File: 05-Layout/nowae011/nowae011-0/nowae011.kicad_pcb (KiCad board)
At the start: 2 copper layers, 25.4 x 18.4 mm, 15 parts, among them P1 VIN, P2 VOUT, U1 ST1S14PHR

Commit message: Updated pcb (nowae011-0)
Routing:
- net Net-(P2-Pad2): track 0.00 -> 1.76 mm
- net +5V: track 14.0 -> 15.8 mm
- net GND: track 17.8 -> 19.2 mm
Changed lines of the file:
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@@
     (thickness 1.6)
     (drawings 30)
-    (tracks 52)
+    (tracks 55)
     (zones 0)
     (modules 15)
@@
     (0 F.Cu signal)
     (31 B.Cu signal)
-    (32 B.Adhes user hide)
-    (33 F.Adhes user hide)
-    (34 B.Paste user hide)
-    (35 F.Paste user hide)
+    (32 B.Adhes user)
+    (33 F.Adhes user)
+    (34 B.Paste user)
+    (35 F.Paste user)
     (36 B.SilkS user)
     (37 F.SilkS user)
-    (38 B.Mask user hide)
-    (39 F.Mask user hide)
+    (38 B.Mask user)
+    (39 F.Mask user)
     (40 Dwgs.User user)
-    (41 Cmts.User user hide)
-    (42 Eco1.User user hide)
-    (43 Eco2.User user hide)
+    (41 Cmts.User user)
+    (42 Eco1.User user)
+    (43 Eco2.User user)
     (44 Edge.Cuts user)
-    (45 Margin user hide)
-    (46 B.CrtYd user hide)
-    (47 F.CrtYd user hide)
-    (48 B.Fab user hide)
+    (45 Margin user)
+    (46 B.CrtYd user)
+    (47 F.CrtYd user)
+    (48 B.Fab user)
     (49 F.Fab user)
   )
   (setup
-    (last_trace_width 0.25)
+    (last_trace_width 1)
     (user_trace_width 0.25)
     (user_trace_width 0.5)
@@
   (gr_line (start 25.4 -13.335) (end 25.4 -5.715) (layer Edge.Cuts) (width 0.15))
   (gr_line (start 0 -5.715) (end 0 -13.335) (layer Edge.Cuts) (width 0.15))
-  (segment (start 2.54 -12.085) (end 0.40001 -12.085) (width 0.25) (layer F.Cu) (net 1))
+  (segment (start 2.54 -12.085) (end 0.77501 -12.085) (width 1) (layer F.Cu) (net 1))
   (via (at 8.255 -6.985) (size 0.6) (drill 0.3) (layers F.Cu B.Cu) (net 2) (status 40000))
   (via (at 10.287 -6.985) (size 0.6) (drill 0.3) (layers F.Cu B.Cu) (net 2) (status 40000))
@@
   (segment (start 2.74 -6.805) (end 2.54 -7.005) (width 1) (layer F.Cu) (net 2))
   (segment (start 4.953 -6.805) (end 2.74 -6.805) (width 1) (layer F.Cu) (net 2))
-  (segment (start 2.54 -7.005) (end 0.40001 -7.005) (width 0.25) (layer F.Cu) (net 2))
   (segment (start 19.217 -16.343) (end 20.32 -15.24) (width 1) (layer F.Cu) (net 2))
   (via (at 20.32 -15.24) (size 1.2) (drill 0.6) (layers F.Cu B.Cu) (net 2))
@@
   (segment (start 6.571 -9.525) (end 8.255 -9.525) (width 0.5) (layer F.Cu) (net 2))
   (segment (start 11.971 -9.525) (end 10.287 -9.525) (width 0.5) (layer F.Cu) (net 2))
+  (segment (start 22.86 -6.965) (end 24.62499 -6.965) (width 1) (layer F.Cu) (net 2))
+  (segment (start 2.54 -7.005) (end 0.77501 -7.005) (width 1) (layer F.Cu) (net 2))
   (segment (start 11.971 -6.985) (end 11.971 -6.185) (width 0.5) (layer F.Cu) (net 3))
   (segment (start 11.971 -6.153) (end 11.971 -6.185) (width 0.5) (layer F.Cu) (net 3))
@@
   (segment (start 15.327 -11.343) (end 14.605 -12.065) (width 0.25) (layer F.Cu) (net 5))
   (segment (start 14.605 -13.6875) (end 13.6255 -14.667) (width 0.25) (layer F.Cu) (net 5))
+  (segment (start 22.86 -12.045) (end 24.62499 -12.045) (width 1) (layer F.Cu) (net 5))
   (segment (start 13.5255 -16.067) (end 12.319 -16.067) (width 0.25) (layer F.Cu) (net 6))
-  (segment (start 2.54 -9.545) (end 0.40001 -9.545) (width 0.25) (layer F.Cu) (net 7))
+  (segment (start 2.54 -9.545) (end 0.77501 -9.545) (width 1) (layer F.Cu) (net 7))
+  (segment (start 22.86 -9.505) (end 24.62499 -9.505) (width 1) (layer F.Cu) (net 8))
   (segment (start 13.4605 -10.795) (end 13.5255 -10.86) (width 0.25) (layer F.Cu) (net 9))
   (segment (start 11.971 -10.795) (end 13.4605 -10.795) (width 0.25) (layer F.Cu) (net 9))
@@
     (connect_pads yes (clearance 0.508))
     (min_thickness 0.254)
-    (fill yes (arc_segments 16) (thermal_gap 0.508) (thermal_bridge_width 0.508))
+    (fill (arc_segments 16) (thermal_gap 0.508) (thermal_bridge_width 0.508))
     (polygon
       (pts
@@
     (connect_pads yes (clearance 0.508))
     (min_thickness 0.254)
-    (fill yes (arc_segments 16) (thermal_gap 0.508) (thermal_bridge_width 0.508))
+    (fill (arc_segments 16) (thermal_gap 0.508) (thermal_bridge_width 0.508))
     (polygon
       (pts
@@
     (connect_pads yes (clearance 0.508))
     (min_thickness 0.254)
-    (fill yes (arc_segments 16) (thermal_gap 0.508) (thermal_bridge_width 0.508))
+    (fill (arc_segments 16) (thermal_gap 0.508) (thermal_bridge_width 0.508))
     (polygon
       (pts
@@
     (connect_pads yes (clearance 0.508))
     (min_thickness 0.254)
-    (fill yes (arc_segments 16) (thermal_gap 0.508) (thermal_bridge_width 0.508))
+    (fill (arc_segments 16) (thermal_gap 0.508) (thermal_bridge_width 0.508))
     (polygon
       (pts

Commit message: WiP: placement silkscreen (nowae011-0)
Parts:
- added G***: LOGO, EXTLOGO:LOGO_OSH_10MM_FSILK, B.Cu at (12.7, -9.53)
- added G***: LOGO, EXTLOGO:LOGO_CC-BY-SA_10MM_FSILK, B.Cu at (12.7, -2.03)
- moved G*** 0.64 mm to (13.0, -16.5)
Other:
- board text added: "NOWAE011-0"

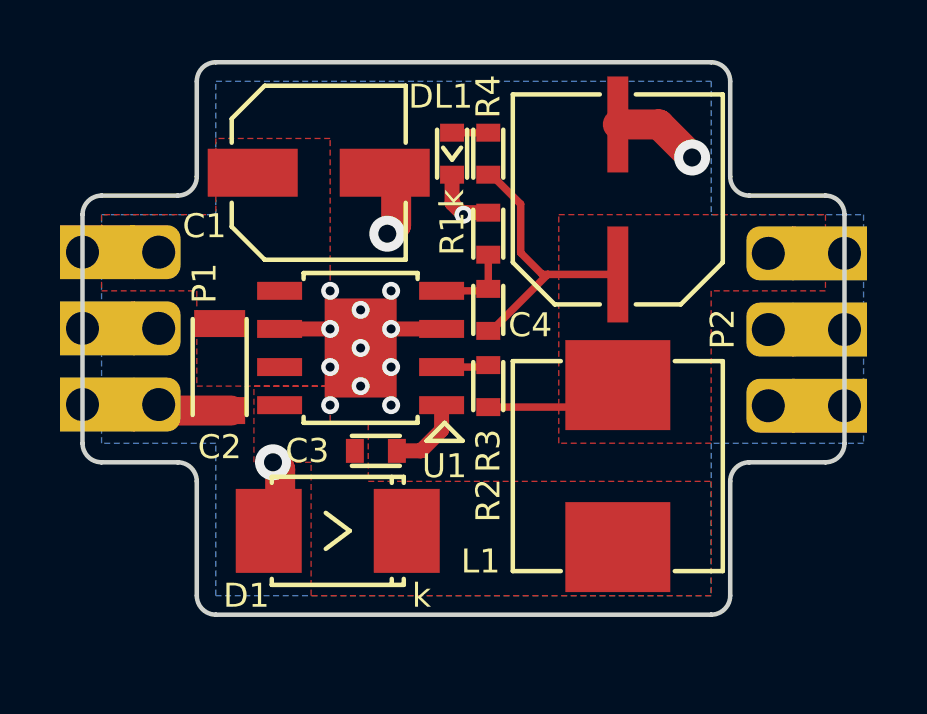
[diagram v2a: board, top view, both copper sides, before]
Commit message: Updated netlist (nowae011-0) WiP: placement components (nowae011-0)
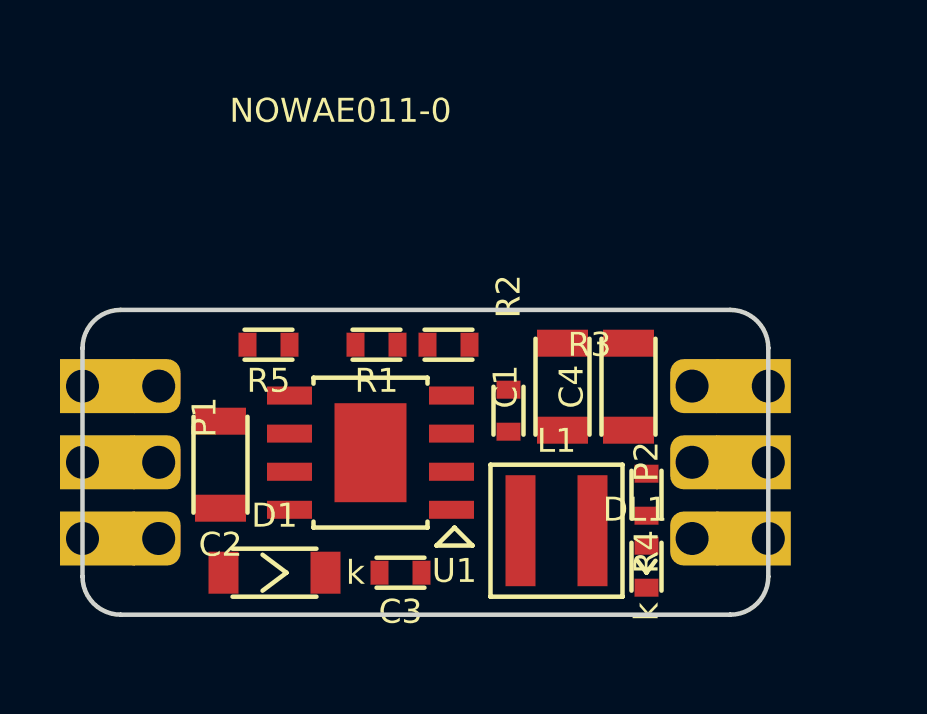
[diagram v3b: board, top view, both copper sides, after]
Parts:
- removed G***: LOGO, LOGO:LOGO_NOWAE_15MM_FSILK
- removed G***: LOGO, EXTLOGO:LOGO_OSH_10MM_FSILK
- removed G***: LOGO, EXTLOGO:LOGO_CC-BY-SA_10MM_FSILK
- added R5: 100k, RESISTOR:RESISTOR-0603, F.Cu at (6.20, -9.00)
- C1: footprint CAPACITOR:CAPACITOR-5.0x5.5 -> CAPACITOR:CAPACITOR-1206
- C2: value 100n -> 4u7
- C4: value 100u -> 10u; footprint CAPACITOR:CAPACITOR-6.3x5.3 -> CAPACITOR:CAPACITOR-1206
- D1: value MBRS2040L -> SS36FA; footprint DIODE:DIODE-DO214AA-UNI -> DIODE:DIODE-SOD123
- L1: footprint INDUCTOR:INDUCTOR-7050 -> INDUCTOR:INDUCTOR-WURTH-4030
- moved DL1 15.2 mm to (18.8, -1.60)
- moved R4 12.5 mm to (18.8, -4.00), turned to 90 degrees
- moved C1 10.8 mm to (16.0, -7.60), turned to 90 degrees
- moved C4 6.25 mm to (18.2, -7.60)
- moved R1 5.25 mm to (9.80, -9.00), turned to 180 degrees
- moved P2 5.10 mm to (21.6, -5.10)
- moved P1 4.47 mm to (1.27, -5.06)
- moved C3 4.14 mm to (10.6, -1.40)
- moved U1 3.51 mm to (9.60, -5.40)
- moved C2 3.26 mm to (4.60, -5.00)
- moved L1 2.97 mm to (15.8, -2.80), turned to 0 degrees
- moved D1 2.53 mm to (6.40, -1.40)
- moved R3 1.76 mm to (12.2, -9.00), turned to 180 degrees
- moved R2 1.06 mm to (14.2, -6.80), turned to 270 degrees
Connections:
- C1 pad 1: +24V -> +5V
- P1 pad 2: Net-(P1-Pad2) -> /EN2
- P2 pad 2: Net-(P2-Pad2) -> /~PG
- R2 pad 2: Net-(R2-Pad2) -> /~PG
- U1 pad 2: Net-(R2-Pad2) -> /~PG
- U1 pad 5: +24V -> /EN2
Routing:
- net GND: track 19.2 -> 0.00 mm, vias 15 -> 0
- net +5V: track 15.8 -> 0.00 mm
- net Net-(R1-Pad1): track 2.72 -> 0.00 mm
- net Net-(C3-Pad1): track 2.61 -> 0.00 mm
- net Net-(P2-Pad2): track 1.76 -> 0.00 mm
- net Net-(P1-Pad2): track 1.76 -> 0.00 mm
- net +24V: track 1.76 -> 0.00 mm
- net Net-(R2-Pad2): track 1.58 -> 0.00 mm
- net Net-(DL1-Pad1): track 1.21 -> 0.00 mm
- removed copper zone on F.Cu, net +24V
- removed copper zone on F.Cu, net +5V
- removed copper zone on B.Cu, net GND
- removed copper zone on F.Cu, net Net-(C3-Pad2)
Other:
- board size 25.4 x 18.4 mm -> 22.9 x 10.2 mm

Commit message: Updated schematic, netfile (nowae011-0) WiP: placement components (nowae011-0)
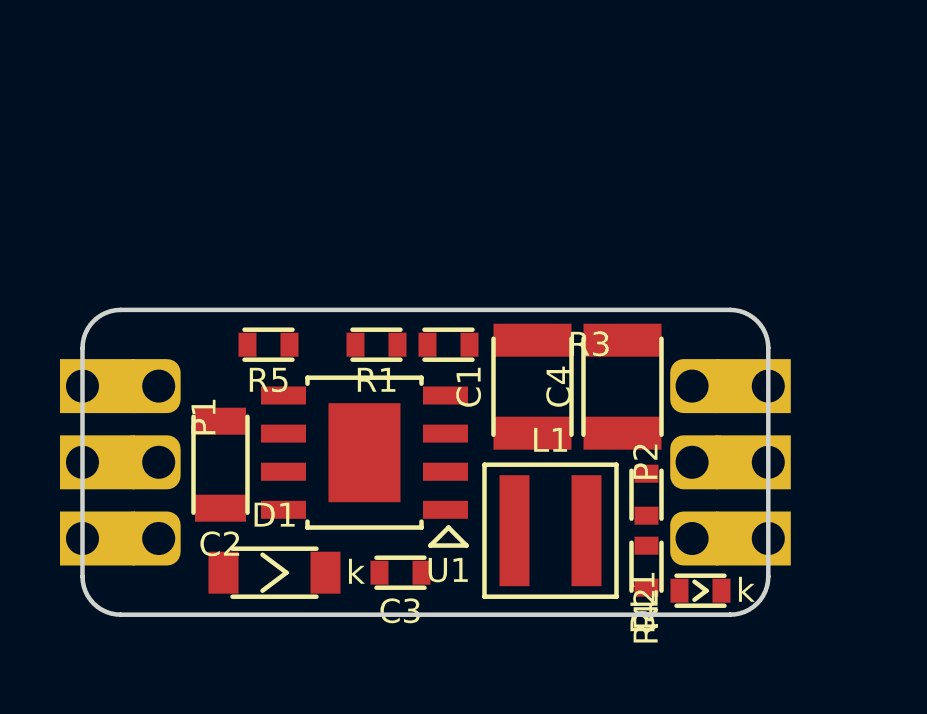
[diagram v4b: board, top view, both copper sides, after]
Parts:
- C1, C4: footprint CAPACITOR:CAPACITOR-1206 -> CAPACITOR:CAPACITOR-1210
- moved R2 5.39 mm to (18.8, -4.00), turned to 90 degrees
- moved R4 2.40 mm to (18.8, -1.60)
- moved DL1 1.97 mm to (20.6, -0.80), turned to 0 degrees
- moved C1 1.00 mm to (15.0, -7.60)
- moved L1 0.20 mm to (15.6, -2.80)
- moved C4 0.20 mm to (18.0, -7.60)
- moved U1 0.20 mm to (9.40, -5.40)
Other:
- board text removed: "+24V"
- board text removed: "+5V"
- board text removed: "GND"
- board text removed: "NOWAE011-0"

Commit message: WiP: placement wires (nowae011-0)
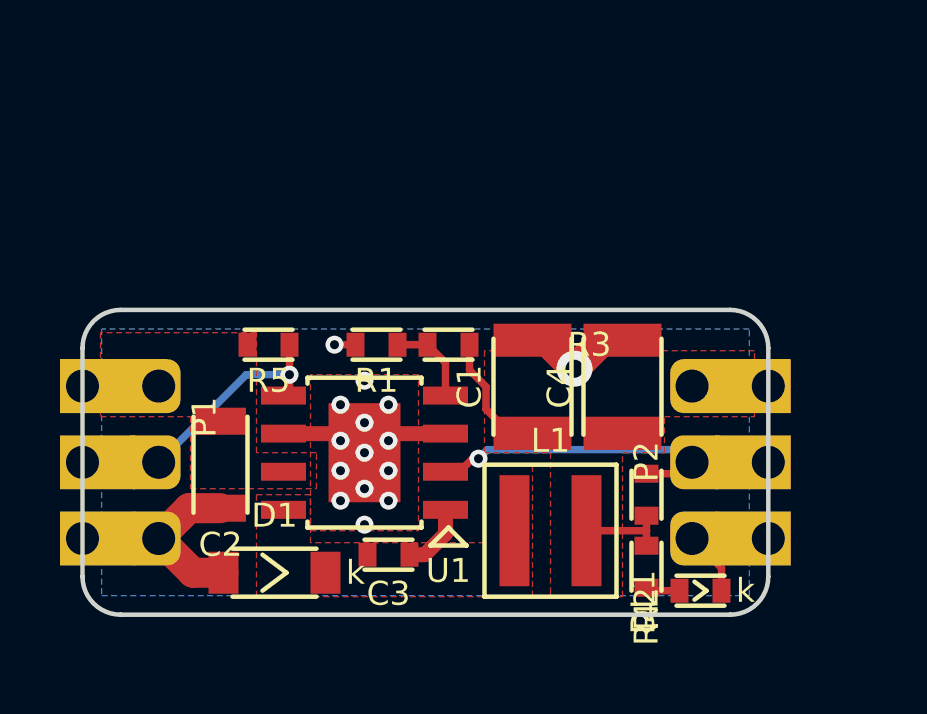
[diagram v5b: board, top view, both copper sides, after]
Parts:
- moved C3 0.72 mm to (10.2, -2.00)
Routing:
- net GND: track 0.00 -> 19.3 mm, vias 0 -> 15
- net /~PG: track 0.00 -> 12.1 mm, vias 0 -> 1
- net /EN2: track 0.00 -> 9.11 mm, vias 0 -> 1
- net +5V: track 0.00 -> 9.02 mm
- net Net-(R1-Pad1): track 0.00 -> 2.94 mm
- net Net-(C3-Pad1): track 0.00 -> 2.29 mm
- net +24V: track 0.00 -> 1.76 mm
- net Net-(DL1-Pad1): track 0.00 -> 1.14 mm
- added copper zone on F.Cu, net +24V
- added copper zone on F.Cu, net +5V
- added copper zone on B.Cu, net GND
- added copper zone on F.Cu, net GND
- added copper zone on F.Cu, net Net-(C3-Pad2)
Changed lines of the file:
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@@
     (thickness 1.6)
     (drawings 10)
-    (tracks 0)
+    (tracks 67)
     (zones 0)
     (modules 15)
@@
   )
   (setup
-    (last_trace_width 0.25)
+    (last_trace_width 0.5)
     (user_trace_width 0.25)
     (user_trace_width 0.5)
     (user_trace_width 1)
     (trace_clearance 0.2)
-    (zone_clearance 0.508)
+    (zone_clearance 0.381)
     (zone_45_only no)
     (trace_min 0.2)
@@
   )
   (module CAPACITOR:CAPACITOR-0603 (layer F.Cu)
-    (at 10.6 -1.4 180)
+    (at 10.2 -2 180)
     (descr "SMD CAP 0603")
     (tags "0603 SM0603")
@@
     (arrow2b (pts (xy 0 3.175) (xy 1.126504 2.588579)))
   )
+  (segment (start 2.54 -7.62) (end 0.77501 -7.62) (width 1) (layer F.Cu) (net 1))
+  (via (at 8.6 -3.8) (size 0.6) (drill 0.3) (layers F.Cu B.Cu) (net 2))
+  (via (at 10.2 -3.8) (size 0.6) (drill 0.3) (layers F.Cu B.Cu) (net 2))
+  (via (at 10.2 -7) (size 0.6) (drill 0.3) (layers F.Cu B.Cu) (net 2))
+  (via (at 8.6 -7) (size 0.6) (drill 0.3) (layers F.Cu B.Cu) (net 2))
+  (via (at 9.4 -6.4) (size 0.6) (drill 0.3) (layers F.Cu B.Cu) (net 2))
+  (via (at 9.4 -4.2) (size 0.6) (drill 0.3) (layers F.Cu B.Cu) (net 2))
+  (via (at 8.6 -4.8) (size 0.6) (drill 0.3) (layers F.Cu B.Cu) (net 2))
+  (via (at 10.2 -4.8) (size 0.6) (drill 0.3) (layers F.Cu B.Cu) (net 2))
+  (via (at 10.2 -5.8) (size 0.6) (drill 0.3) (layers F.Cu B.Cu) (net 2))
+  (via (at 8.6 -5.8) (size 0.6) (drill 0.3) (layers F.Cu B.Cu) (net 2))
+  (segment (start 3.68 -1.4) (end 2.54 -2.54) (width 1) (layer F.Cu) (net 2))
+  (segment (start 4.7 -1.4) (end 3.68 -1.4) (width 1) (layer F.Cu) (net 2))
+  (segment (start 3.55 -3.55) (end 2.54 -2.54) (width 1) (layer F.Cu) (net 2))
+  (segment (start 4.6 -3.55) (end 3.55 -3.55) (width 1) (layer F.Cu) (net 2))
+  (segment (start 15 -9.15) (end 15.45 -9.15) (width 1) (layer F.Cu) (net 2))
+  (via (at 16.4 -8.2) (size 1.2) (drill 0.6) (layers F.Cu B.Cu) (net 2))
+  (segment (start 15.45 -9.15) (end 16.4 -8.2) (width 1) (layer F.Cu) (net 2))
+  (segment (start 17.35 -9.15) (end 16.4 -8.2) (width 1) (layer F.Cu) (net 2))
+  (segment (start 18 -9.15) (end 17.35 -9.15) (width 1) (layer F.Cu) (net 2))
+  (segment (start 9.1 -9) (end 8.4 -9) (width 0.25) (layer F.Cu) (net 2))
+  (via (at 8.4 -9) (size 0.6) (drill 0.3) (layers F.Cu B.Cu) (net 2))
+  (via (at 9.4 -5.4) (size 0.6) (drill 0.3) (layers F.Cu B.Cu) (net 2))
+  (segment (start 10.435 -6.035) (end 10.2 -5.8) (width 0.5) (layer F.Cu) (net 2))
+  (segment (start 12.1 -6.035) (end 10.435 -6.035) (width 0.5) (layer F.Cu) (net 2))
+  (segment (start 8.365 -6.035) (end 8.6 -5.8) (width 0.5) (layer F.Cu) (net 2))
+  (segment (start 6.7 -6.035) (end 8.365 -6.035) (width 0.5) (layer F.Cu) (net 2))
+  (segment (start 21.3 -1.56) (end 20.32 -2.54) (width 0.25) (layer F.Cu) (net 2))
+  (segment (start 21.3 -0.8) (end 21.3 -1.56) (width 0.25) (layer F.Cu) (net 2))
+  (segment (start 20.32 -2.54) (end 22.08499 -2.54) (width 1) (layer F.Cu) (net 2))
+  (segment (start 2.54 -2.54) (end 0.77501 -2.54) (width 1) (layer F.Cu) (net 2))
+  (via (at 9.4 -7.8) (size 0.6) (drill 0.3) (layers F.Cu B.Cu) (net 2))
+  (via (at 9.4 -3) (size 0.6) (drill 0.3) (layers F.Cu B.Cu) (net 2))
+  (segment (start 12.1 -2.695) (end 11.405 -2) (width 0.5) (layer F.Cu) (net 3))
+  (segment (start 12.1 -3.495) (end 12.1 -2.695) (width 0.5) (layer F.Cu) (net 3))
+  (segment (start 11.405 -2) (end 10.9 -2) (width 0.5) (layer F.Cu) (net 3))
+  (segment (start 13.45 -6.85) (end 14.25 -6.05) (width 0.25) (layer F.Cu) (net 5))
+  (segment (start 13.45 -7.6) (end 13.45 -6.85) (width 0.25) (layer F.Cu) (net 5))
+  (segment (start 14.25 -6.05) (end 15 -6.05) (width 0.25) (layer F.Cu) (net 5))
+  (segment (start 12.9 -8.15) (end 13.45 -7.6) (width 0.25) (layer F.Cu) (net 5))
+  (segment (start 12.9 -9) (end 12.9 -8.15) (width 0.25) (layer F.Cu) (net 5))
+  (segment (start 16.8 -2.8) (end 18.8 -2.8) (width 0.25) (layer F.Cu) (net 5))
+  (segment (start 18.8 -2.8) (end 18.8 -3.3) (width 0.25) (layer F.Cu) (net 5))
+  (segment (start 18.8 -2.3) (end 18.8 -2.8) (width 0.25) (layer F.Cu) (net 5))
+  (segment (start 20.32 -7.62) (end 22.08499 -7.62) (width 1) (layer F.Cu) (net 5))
+  (segment (start 18.9 -0.8) (end 18.8 -0.9) (width 0.25) (layer F.Cu) (net 6))
+  (segment (start 19.9 -0.8) (end 18.9 -0.8) (width 0.25) (layer F.Cu) (net 6))
+  (segment (start 6.9 -7.505) (end 6.7 -7.305) (width 0.25) (layer F.Cu) (net 7))
+  (segment (start 6.9 -9) (end 6.9 -8) (width 0.25) (layer F.Cu) (net 7))
+  (via (at 6.9 -8) (size 0.6) (drill 0.3) (layers F.Cu B.Cu) (net 7))
+  (segment (start 6.9 -8) (end 6.9 -7.505) (width 0.25) (layer F.Cu) (net 7))
+  (segment (start 5.46 -8) (end 2.54 -5.08) (width 0.25) (layer B.Cu) (net 7))
+  (segment (start 6.9 -8) (end 5.46 -8) (width 0.25) (layer B.Cu) (net 7))
+  (segment (start 2.54 -5.08) (end 0.77501 -5.08) (width 1) (layer F.Cu) (net 7))
+  (segment (start 19.94 -4.7) (end 20.32 -5.08) (width 0.25) (layer F.Cu) (net 8))
+  (segment (start 18.8 -4.7) (end 19.94 -4.7) (width 0.25) (layer F.Cu) (net 8))
+  (segment (start 12.1 -4.765) (end 12.565 -4.765) (width 0.25) (layer F.Cu) (net 8))
+  (via (at 13.2 -5.2) (size 0.6) (drill 0.3) (layers F.Cu B.Cu) (net 8))
+  (segment (start 13 -5.2) (end 13.2 -5.2) (width 0.25) (layer F.Cu) (net 8))
+  (segment (start 12.565 -4.765) (end 13 -5.2) (width 0.25) (layer F.Cu) (net 8))
+  (segment (start 19.900001 -5.499999) (end 20.32 -5.08) (width 0.25) (layer B.Cu) (net 8))
+  (segment (start 13.499999 -5.499999) (end 19.900001 -5.499999) (width 0.25) (layer B.Cu) (net 8))
+  (segment (start 13.2 -5.2) (end 13.499999 -5.499999) (width 0.25) (layer B.Cu) (net 8))
+  (segment (start 20.32 -5.08) (end 22.08499 -5.08) (width 1) (layer F.Cu) (net 8))
+  (segment (start 10.5 -9) (end 11.5 -9) (width 0.25) (layer F.Cu) (net 9))
+  (segment (start 12.1 -8.4) (end 11.5 -9) (width 0.25) (layer F.Cu) (net 9))
+  (segment (start 12.1 -7.305) (end 12.1 -8.4) (width 0.25) (layer F.Cu) (net 9))
+  (zone (net 2) (net_name GND) (layer B.Cu) (hatch edge 0.508)
+    (connect_pads yes (clearance 0.508))
+    (min_thickness 0.254)
+    (fill yes (arc_segments 16) (thermal_gap 0.508) (thermal_bridge_width 0.508))
+    (polygon
+      (pts
+        (xy 0.635 -9.525) (xy 0.635 -0.635) (xy 22.225 -0.635) (xy 22.225 -9.525)
+      )
+    )
+  )
+  (zone (net 1) (net_name +24V) (layer F.Cu) (hatch edge 0.508)
+    (connect_pads yes (clearance 0.508))
+    (min_thickness 0.254)
+    (fill yes (arc_segments 16) (thermal_gap 0.508) (thermal_bridge_width 0.508))
+    (polygon
+      (pts
+        (xy 0.6 -9.4) (xy 0.6 -6.6) (xy 3.6 -6.6) (xy 3.6 -4.2) (xy 7.8 -4.2)
+        (xy 7.8 -5.4) (xy 5.8 -5.4) (xy 5.8 -9.4)
+      )
+    )
+  )
+  (zone (net 5) (net_name +5V) (layer F.Cu) (hatch edge 0.508)
+    (connect_pads yes (clearance 0.508))
+    (min_thickness 0.254)
+    (fill yes (arc_segments 16) (thermal_gap 0.508) (thermal_bridge_width 0.508))
+    (polygon
+      (pts
+        (xy 15.6 -0.6) (xy 18 -0.6) (xy 18 -5.4) (xy 19.4 -5.4) (xy 19.4 -6.6)
+        (xy 22.4 -6.6) (xy 22.4 -8.8) (xy 13.4 -8.8) (xy 13.4 -5.4) (xy 15.6 -5.4)
+        (xy 15.6 -0.8)
+      )
+    )
+  )
+  (zone (net 4) (net_name "Net-(C3-Pad2)") (layer F.Cu) (hatch edge 0.508)
+    (connect_pads yes (clearance 0.381))
+    (min_thickness 0.254)
+    (fill yes (arc_segments 16) (thermal_gap 0.508) (thermal_bridge_width 0.508))
+    (polygon
+      (pts
+        (xy 5.8 -4) (xy 5.8 -0.6) (xy 15 -0.6) (xy 15 -5) (xy 13.4 -5)
+        (xy 13.4 -2.4) (xy 7.6 -2.4) (xy 7.6 -4)
+      )
+    )
+  )
+  (zone (net 2) (net_name GND) (layer F.Cu) (hatch edge 0.508)
+    (connect_pads yes (clearance 0.381))
+    (min_thickness 0.254)
+    (fill yes (arc_segments 16) (thermal_gap 0.508) (thermal_bridge_width 0.508))
+    (polygon
+      (pts
+        (xy 7.6 -8) (xy 7.6 -2.8) (xy 11.2 -2.8) (xy 11.2 -8)
+      )
+    )
+  )
 )
